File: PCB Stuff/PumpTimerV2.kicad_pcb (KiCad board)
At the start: 2 copper layers, 50 x 50 mm, 32 parts, among them J1 1935161, J2 282856-2, J3 282856-2, J4 Conn_02x12_Odd_Even, J5 B6B-PH-SM4-TBT(LF)(SN), J6 B4B-PH-SM4-TBT(LF)(SN), J7 B6B-PH-SM4-TBT(LF)(SN), J8 B4B-PH-SM4-TBT(LF)(SN), K1 ADW1205HLW, K2 ADW1205HLW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

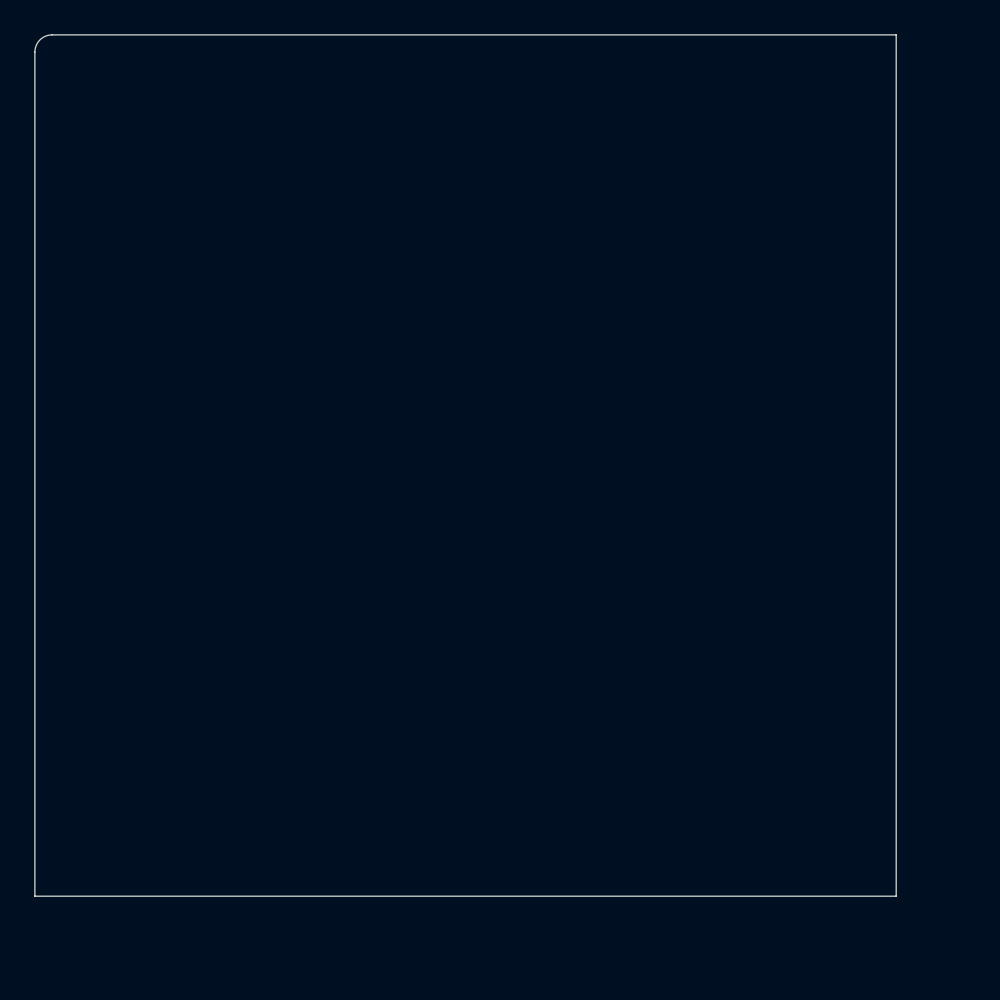
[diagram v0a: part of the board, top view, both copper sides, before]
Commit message: Adding button interface + LED indicator for manual switching of pump state
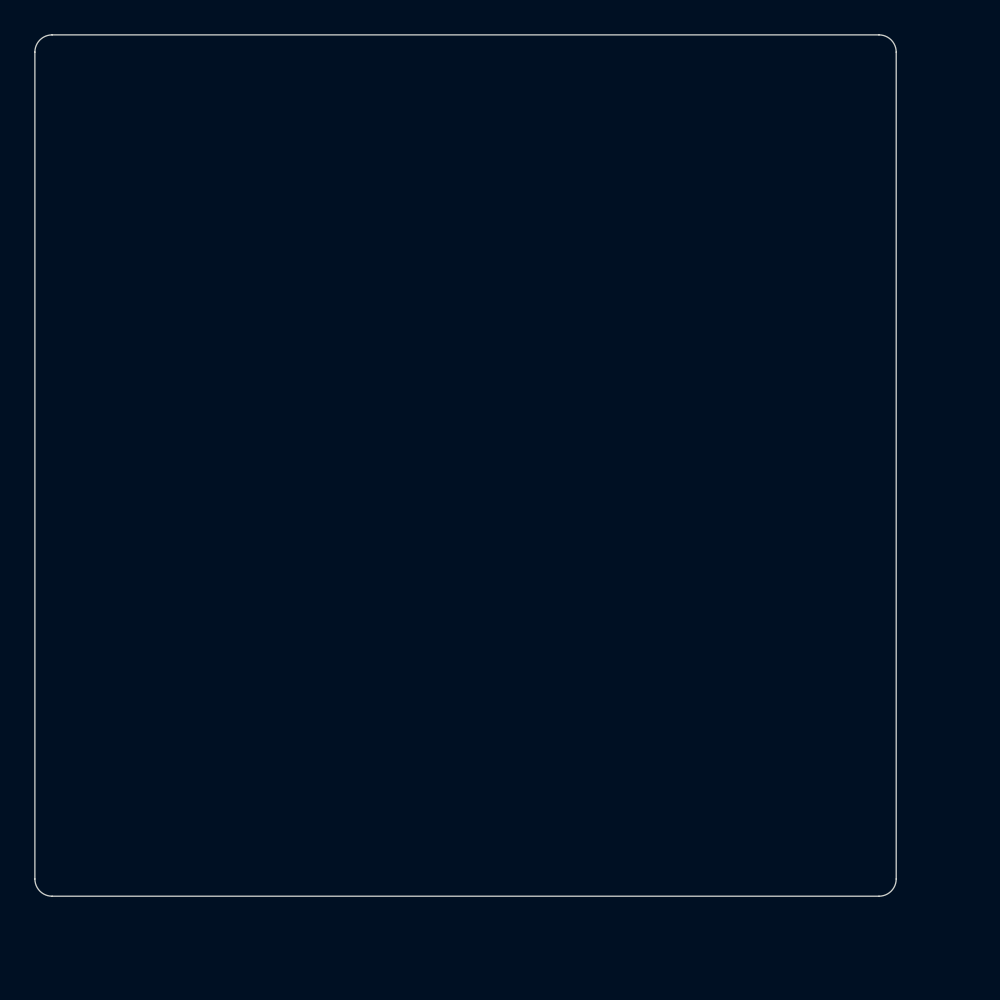
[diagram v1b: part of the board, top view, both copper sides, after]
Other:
- outline, holes or cut-outs redrawn
- copper layers 2 -> 4
- rule pad_to_mask_clearance: 0 -> 0.05

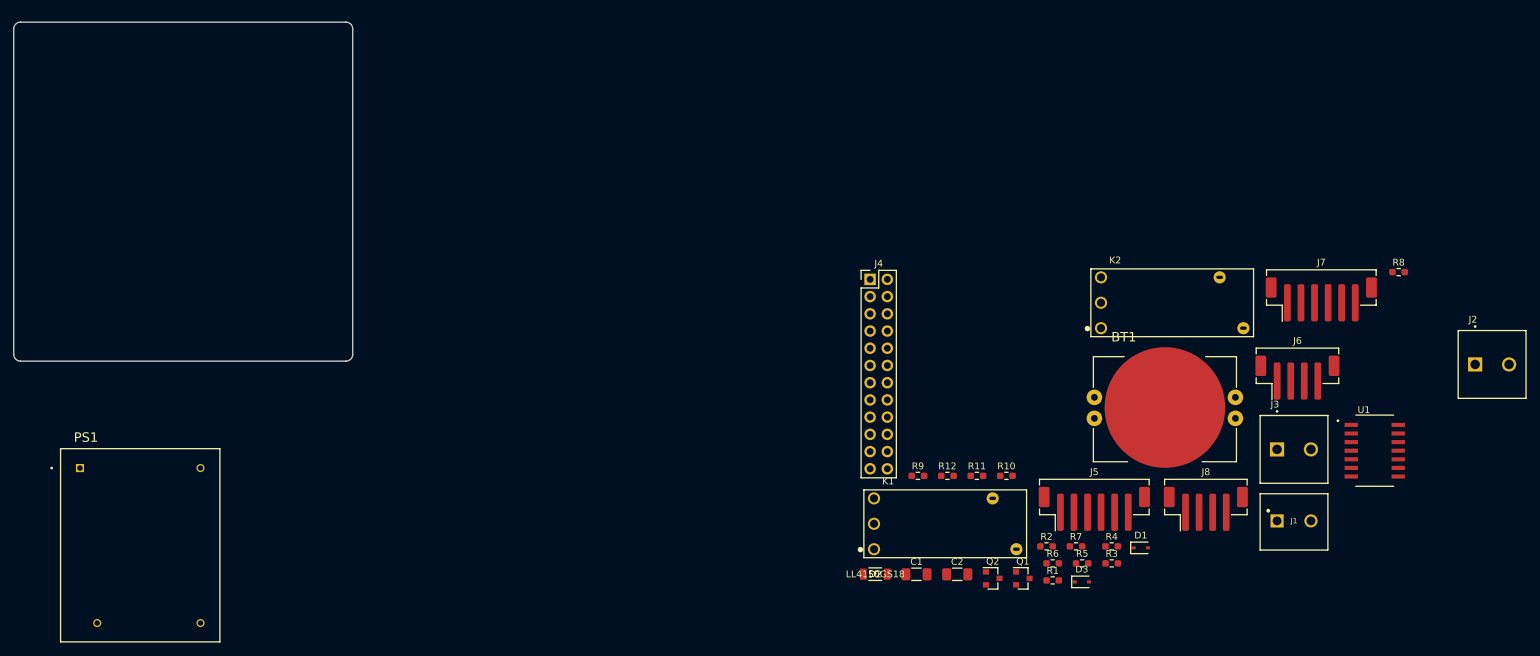
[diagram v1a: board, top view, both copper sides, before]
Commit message: Beginning layout. Removed a few non-critical components that will not fit.
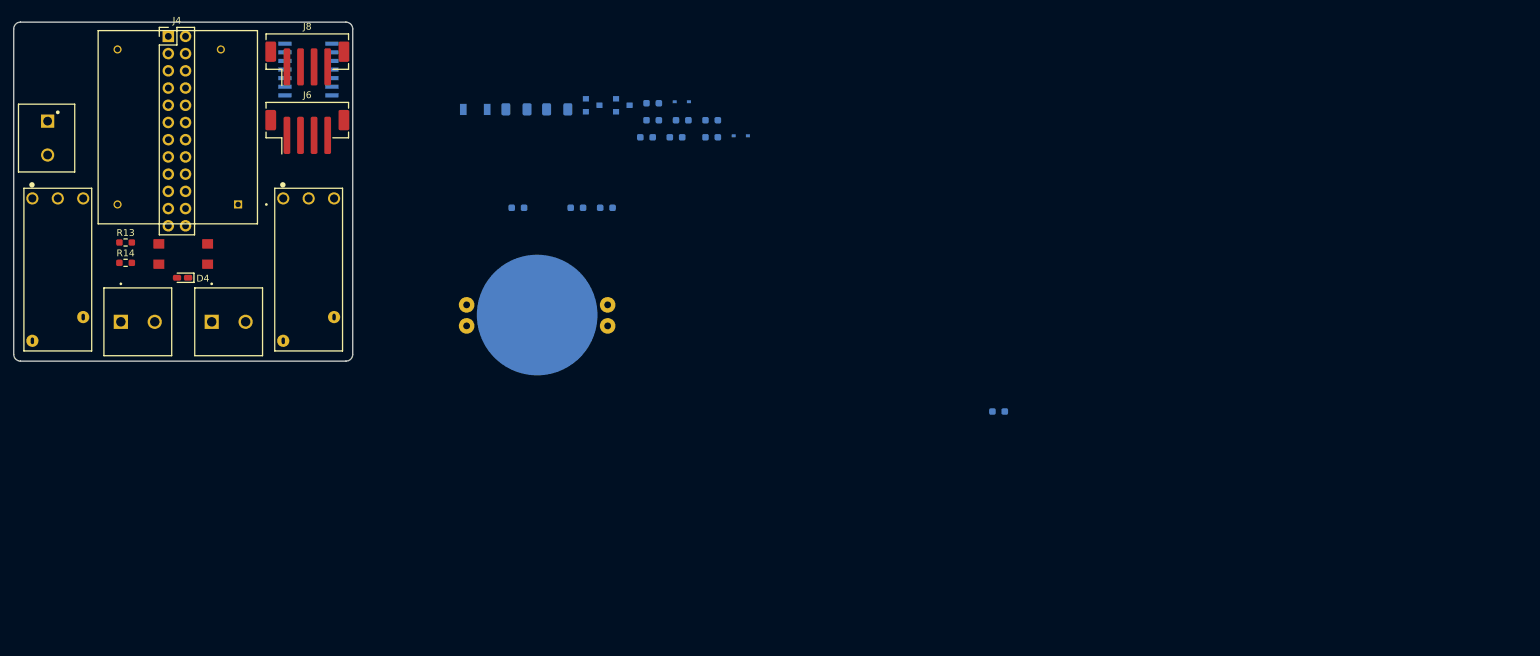
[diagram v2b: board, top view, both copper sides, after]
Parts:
- removed J5, J7: B6B-PH-SM4-TBT(LF)(SN), Connector_JST:JST_PH_B6B-PH-SM4-TB_1x06-1MP_P2.00mm_Vertical
- removed R12: 49.9, Resistor_SMD:R_0603_1608Metric_Pad0.98x0.95mm_HandSolder
- added D4: LED, LED_SMD:LED_0603_1608Metric_Castellated, F.Cu at (79.9, 97.7)
- added R13: 2k2, Resistor_SMD:R_0603_1608Metric_Pad0.98x0.95mm_HandSolder, F.Cu at (71.5, 92.5)
- added R14: 330, Resistor_SMD:R_0603_1608Metric_Pad0.98x0.95mm_HandSolder, F.Cu at (71.5, 95.5)
- added SW1: TL3305AF160QG, Button_Switch_SMD:TL3305AF160QG, F.Cu at (80.0, 94.2)
- BT1, C1, C2, D1, D2, D3, Q1, Q2, R1, R10, R11, R2, R3, R4, R5, R6, R7, R8, R9, U1: moved to B.Cu
- moved J2 199.8 mm to (73.3, 104.2)
- moved J1 192.3 mm to (60.0, 77.1), turned to 270 degrees
- moved U1 164.6 mm to (95.0, 70.8)
- moved J3 158.3 mm to (86.7, 104.2)
- moved J6 150.5 mm to (98.3, 76.2)
- moved J8 147.9 mm to (98.3, 66.1)
- moved K1 136.2 mm to (61.5, 96.5), turned to 270 degrees
- moved K2 127.5 mm to (98.5, 96.5), turned to 270 degrees
- moved J4 109.5 mm to (77.8, 62.1)
- moved BT1 93.6 mm to (132.2, 103.2), turned to 180 degrees
- moved D3 92.2 mm to (153.5, 71.7)
- moved R1 91.8 mm to (149.2, 72.0)
- moved Q1 91.4 mm to (144.8, 72.3)
- moved Q2 91.4 mm to (140.4, 72.3)
- moved C1 90.5 mm to (129.2, 72.9)
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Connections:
- J3 pad 1: /Line2_in -> /Line2_out
- J3 pad 2: /Line2_out -> /Line2_in
- J4 pad 10: Net-(J4-Pad10) -> /~BTN_RDY~
- J6 pad 2: /GPIO2(SDA1) -> /GPIO3(SCL1)
- J6 pad 3: /GPIO3(SCL1) -> /GPIO2(SDA1)
- PS1 pad 1: /Line1_in -> /Line2_in

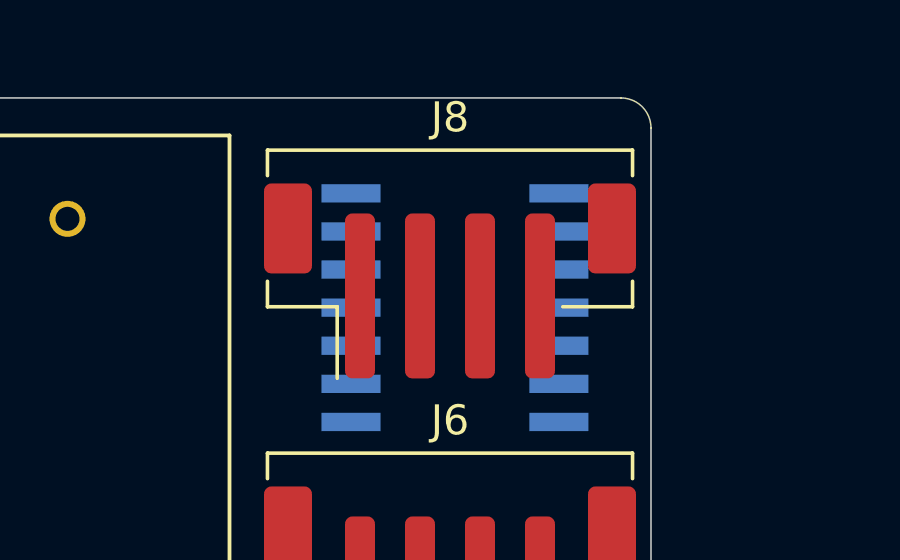
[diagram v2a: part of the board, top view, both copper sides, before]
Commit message: Temoprarily adding 3D models, removing stuff in PCB layout
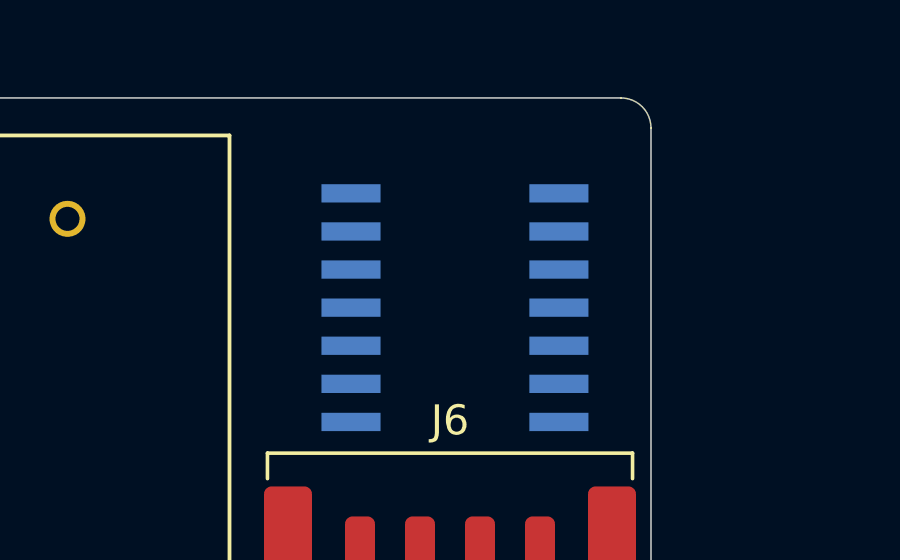
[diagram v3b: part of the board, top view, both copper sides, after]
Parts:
- removed J8: B4B-PH-SM4-TBT(LF)(SN), Connector_JST:JST_PH_B4B-PH-SM4-TB_1x04-1MP_P2.00mm_Vertical

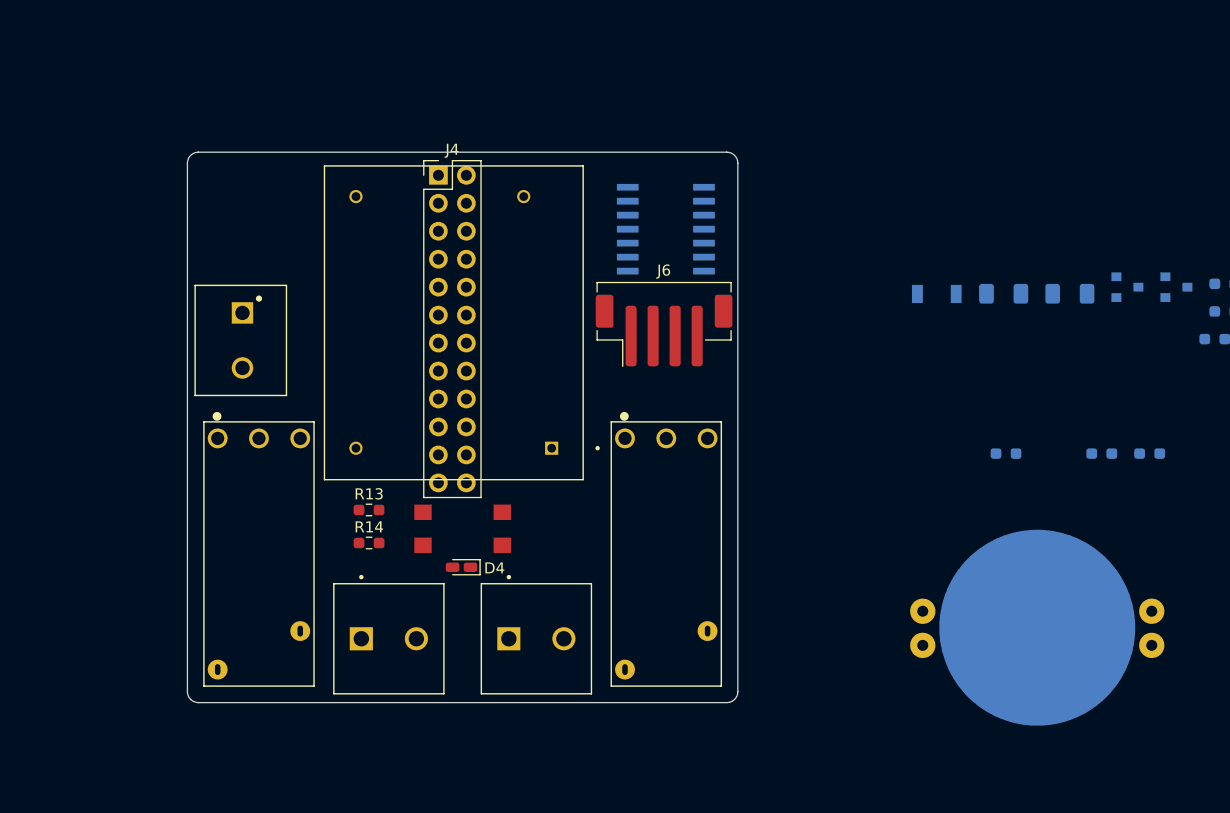
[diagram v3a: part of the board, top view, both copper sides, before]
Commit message: Same as last. Need to flip RPI and connector. Line up for mounting.
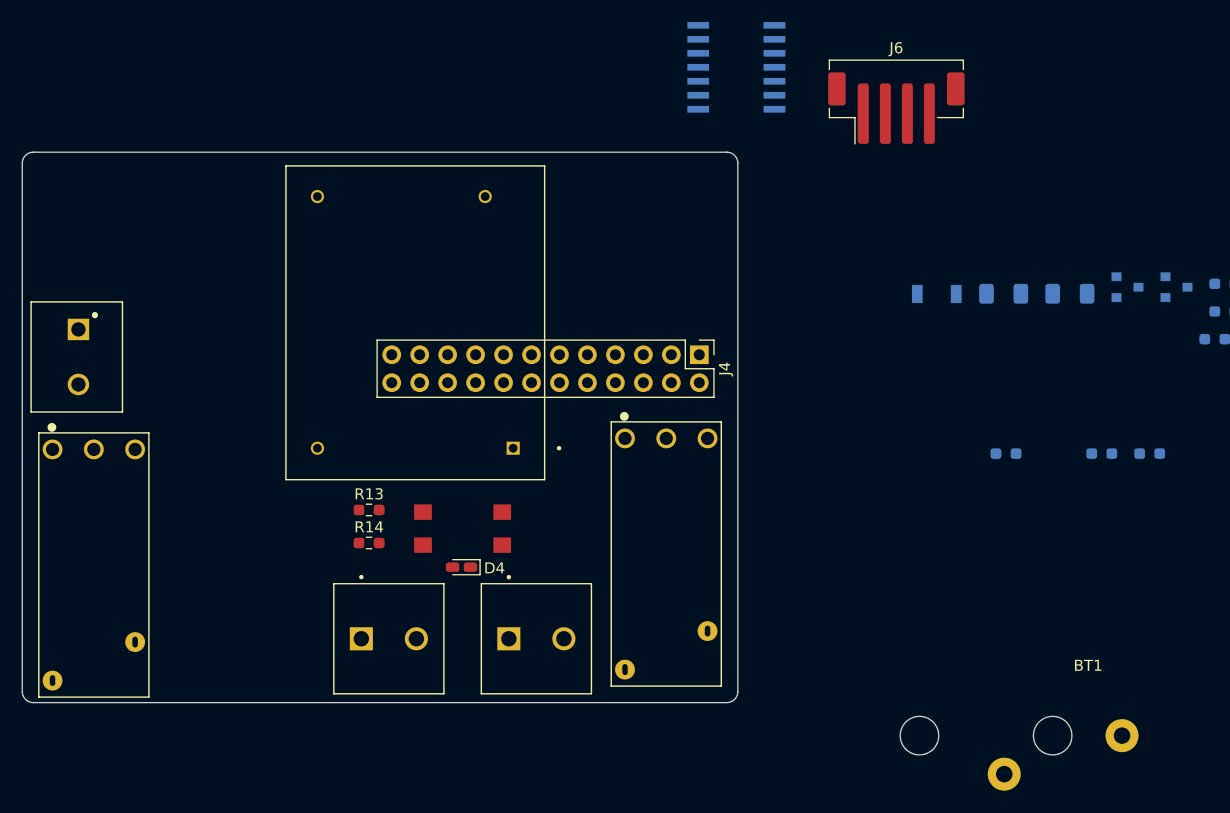
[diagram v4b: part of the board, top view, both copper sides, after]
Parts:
- BT1: value 2032 -> 1632; footprint Battery:BAT_HLD_2032 -> temp:Vertical_16mm_coin; moved to F.Cu
- moved J6 29.2 mm to (119.4, 56.0)
- moved J4 28.8 mm to (101.5, 78.4), turned to 270 degrees
- moved U1 16.0 mm to (101.4, 56.1)
- moved K1 15.0 mm to (46.5, 97.5)
- moved J1 15.0 mm to (45.1, 78.6)
- moved BT1 10.2 mm to (129.2, 113.0), turned to 0 degrees
- moved PS1 3.50 mm to (75.7, 75.5)
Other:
- board size 50 x 50 mm -> 65 x 50 mm

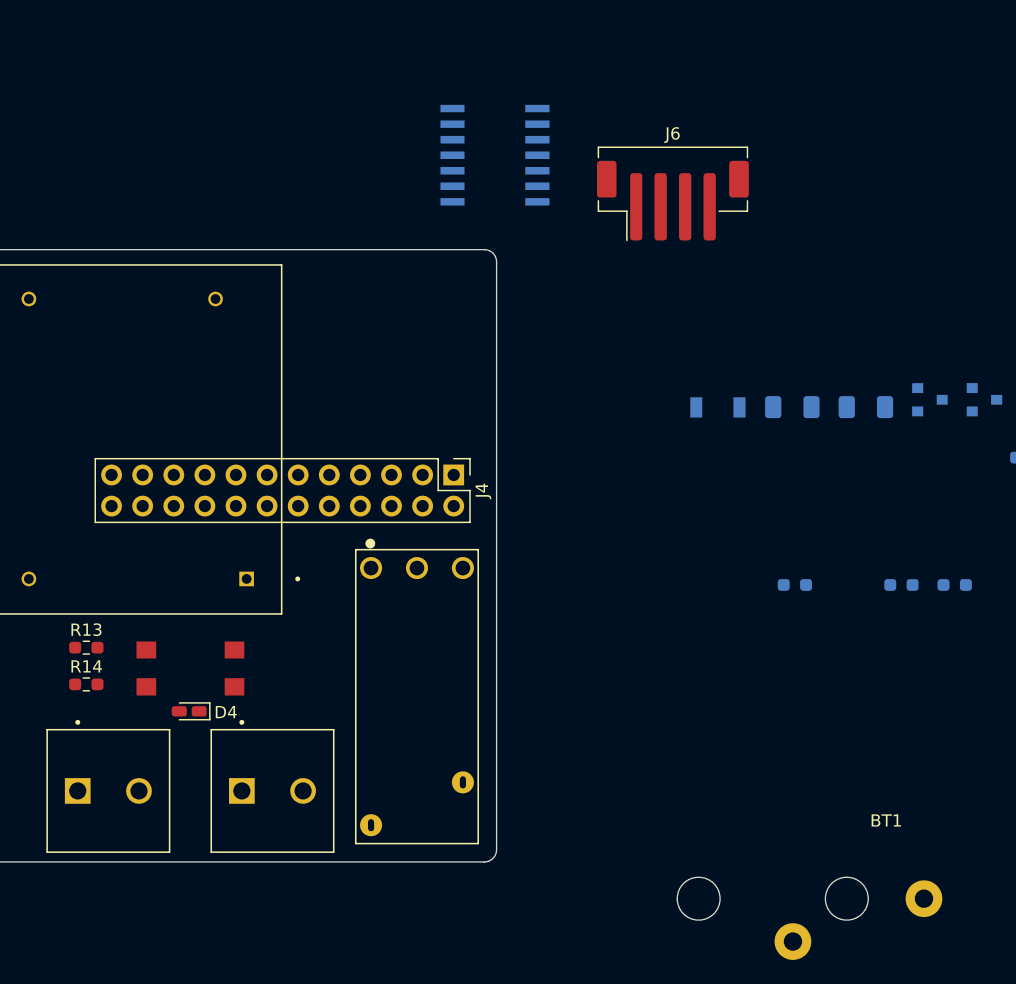
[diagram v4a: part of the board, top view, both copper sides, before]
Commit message: Clean-up, changing board size + adding bigger header for rpi
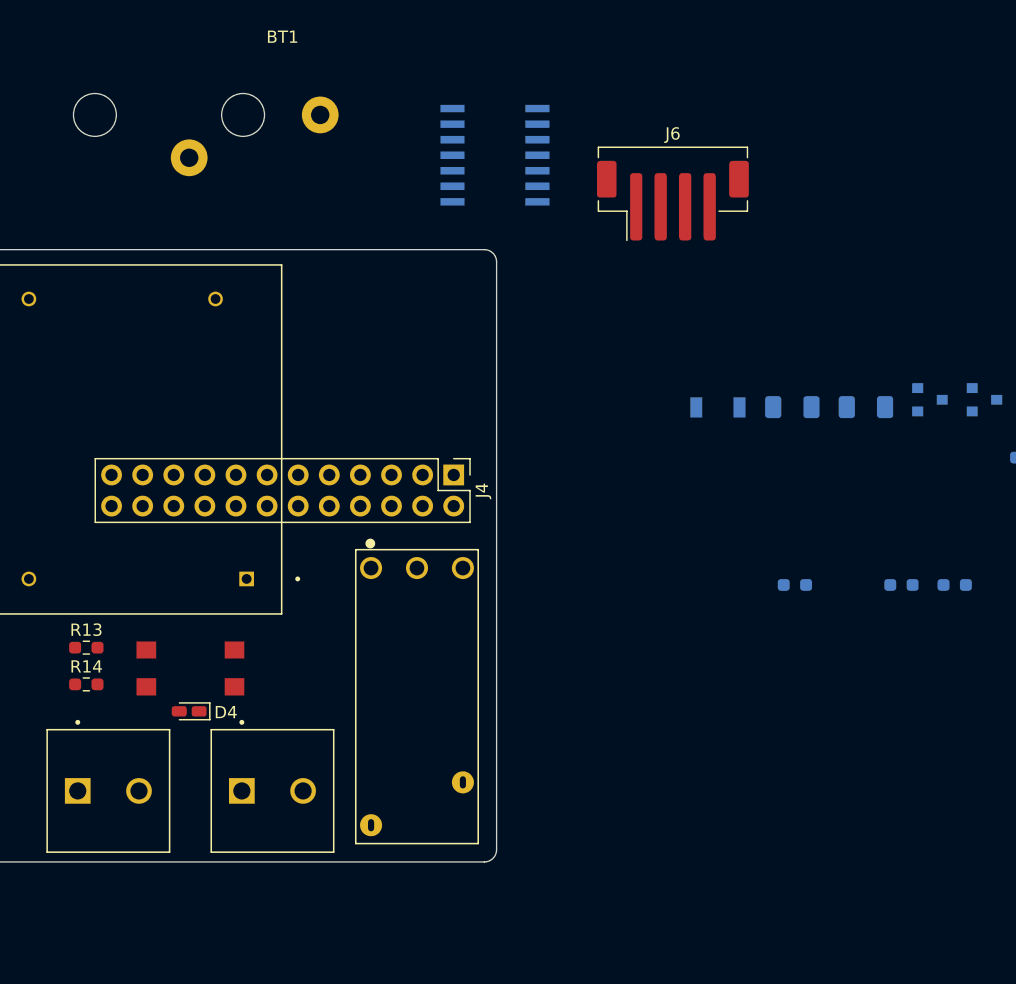
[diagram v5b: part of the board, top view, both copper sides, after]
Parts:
- BT1: footprint temp:Vertical_16mm_coin -> Battery:Vertical_16mm_coin_holder
- J4: value Conn_02x12_Odd_Even -> Conn_02x20_Odd_Even
- moved BT1 80.8 mm to (79.9, 49.0)

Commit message: Work on PCB layout
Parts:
- added J6: B4B-PH-SM4-TBT(LF)(SN), Connector_JST:JST_PH_B4B-PH-SM4-TB_1x04-1MP_P2.00mm_Vertical, F.Cu at (99.5, 77.0)
- J4: footprint Connector_PinHeader_2.54mm:PinHeader_2x12_P2.54mm_Vertical -> Connector_PinHeader_2.54mm:PinHeader_2x20_P2.54mm_Vertical
- moved BT1 54.1 mm to (98.3, 99.9), turned to 90 degrees
- moved SW1 36.6 mm to (44.1, 101.5), turned to 270 degrees
- moved J6 36.5 mm to (89.5, 77.0), turned to 270 degrees
- moved D4 35.8 mm to (44.2, 95.3), turned to 0 degrees
- moved R14 27.4 mm to (44.2, 93.3)
- moved R13 22.1 mm to (52.6, 81.0)
- moved J4 14.0 mm to (96.6, 65.2)
- moved PS1 9.08 mm to (72.5, 84.0)
- moved J2 8.31 mm to (65.0, 104.5)
- moved K1 7.52 mm to (54.0, 97.0)
- moved K2 7.52 mm to (91.0, 97.0)
- moved J3 6.71 mm to (80.0, 104.5)
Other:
- outline, holes or cut-outs redrawn
